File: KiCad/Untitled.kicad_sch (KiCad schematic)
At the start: 1 part

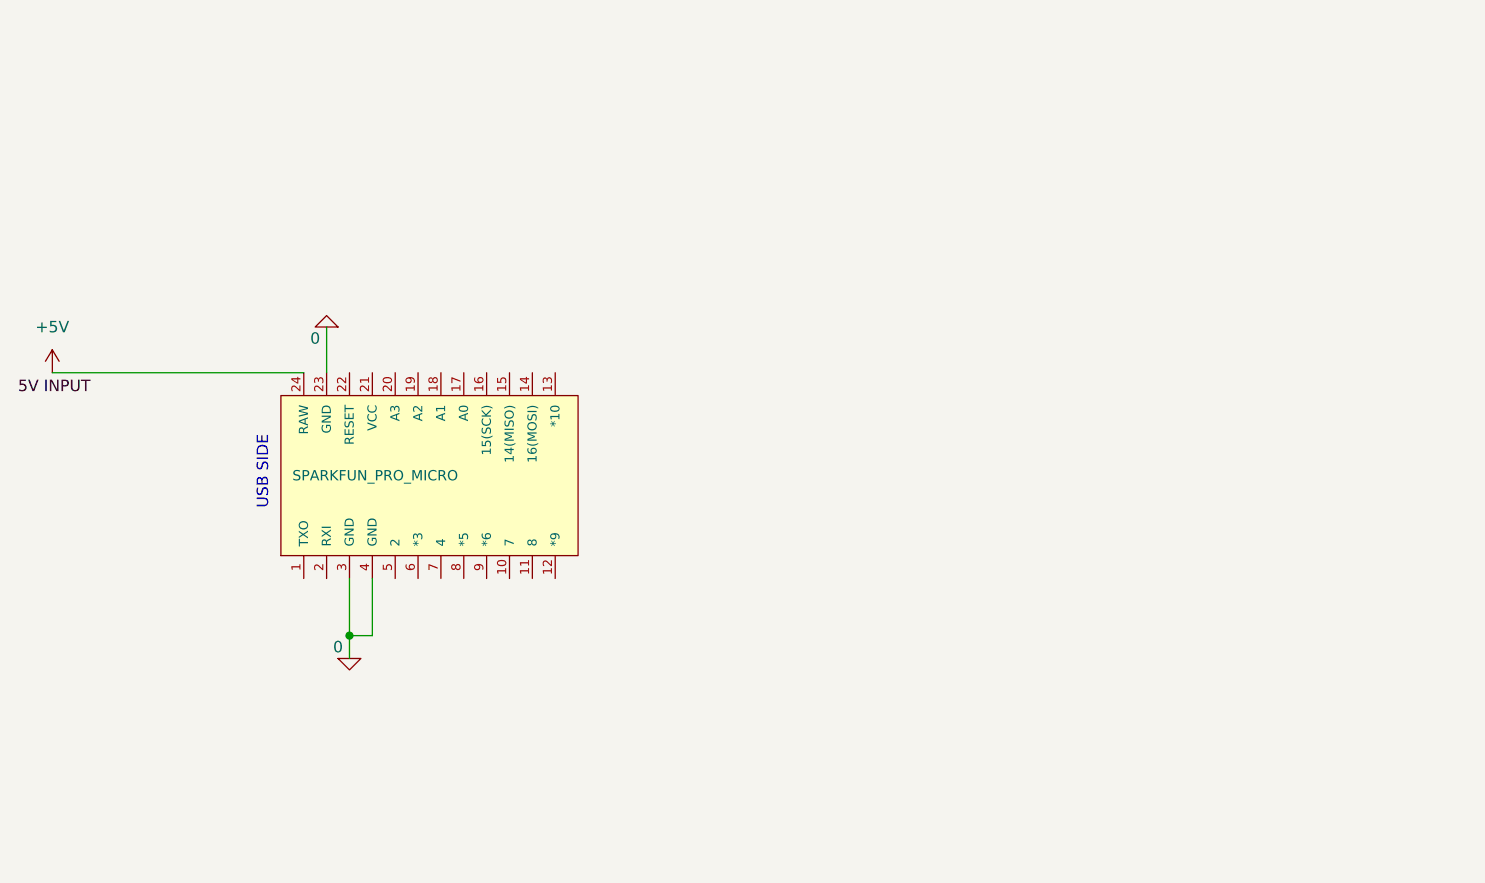
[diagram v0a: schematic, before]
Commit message: update schematics->need to add SSD1302 128x32
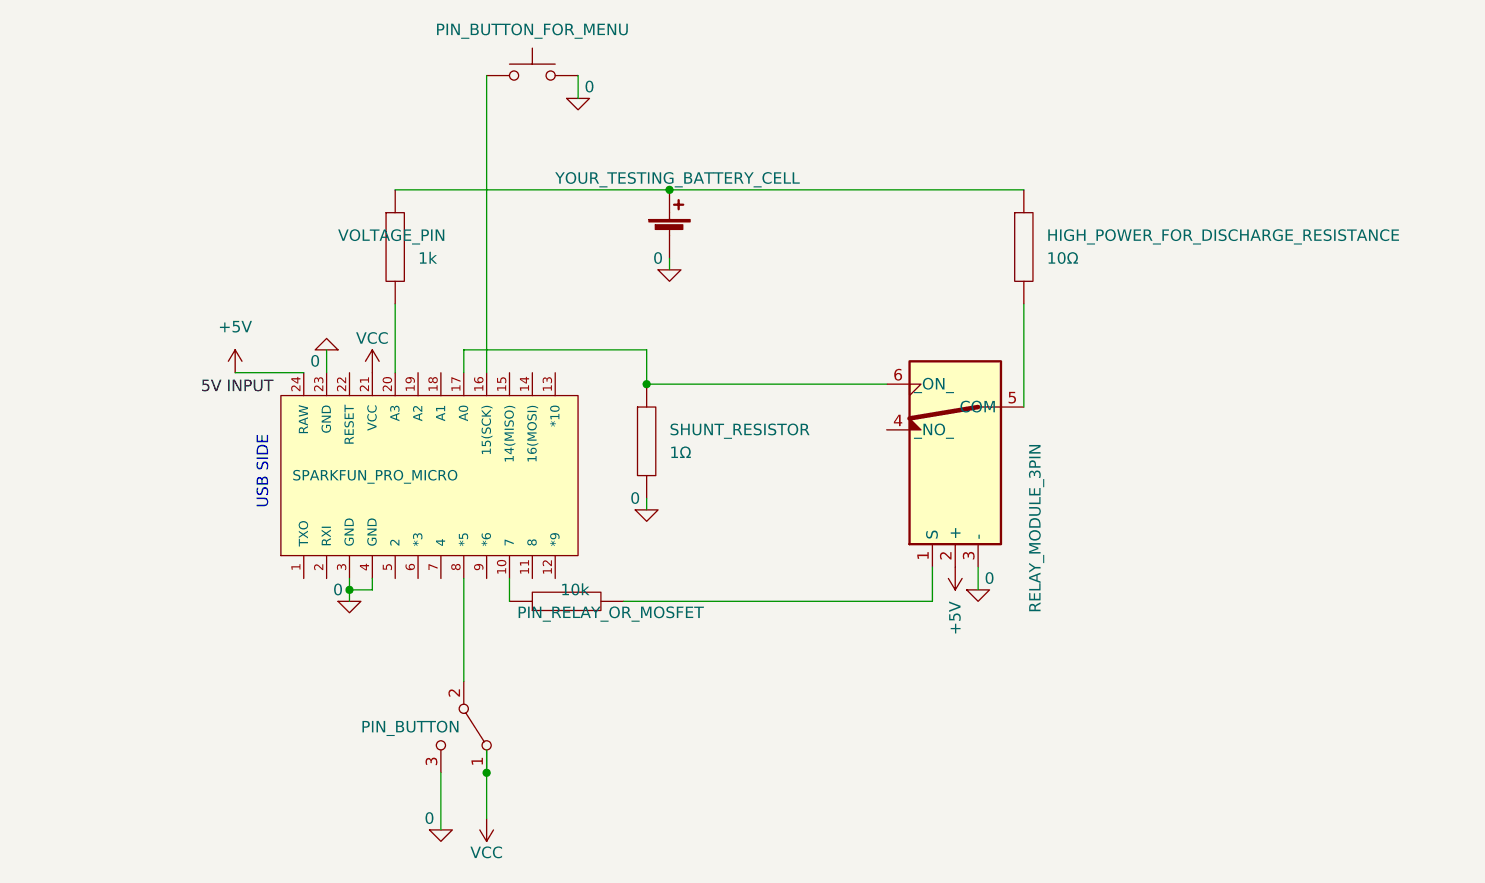
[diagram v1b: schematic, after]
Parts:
- added BT?: YOUR_TESTING_BATTERY_CELL, symbol Device:Battery_Cell
- added HIGH_POWER_FOR_DISCHARGE_RESISTANCE: 10Ω, symbol pspice:R
- added K?: RELAY_MODULE_3PIN, Relay_THT:Relay_StandexMeder_DIP_LowProfile, symbol Relay:DIPxx-1Cxx-51x
- added PIN_BUTTON_: PIN_BUTTON, symbol Switch:SW_DPDT_x2
- added PIN_RELAY_OR_MOSFET: 10k, symbol pspice:R
- added SHUNT_RESISTOR: 1Ω, symbol pspice:R
- added SW?: PIN_BUTTON_FOR_MENU, symbol Switch:SW_MEC_5G
- added VOLTAGE_PIN: 1k, symbol pspice:R
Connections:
- net +5V: now also K?.2 (+)
- net 0: now also BT?.2 (-), K?.3 (-), PIN_BUTTON_.3 (C), SHUNT_RESISTOR.2, SW?.3 (B), SW?.4 (B)
- net at B?.10 (7): now also PIN_RELAY_OR_MOSFET.1
- net at B?.16 (15(SCK)): now also SW?.1 (A), SW?.2 (A)
- net at B?.17 (A0): now also K?.6 (_ON_), SHUNT_RESISTOR.1
- net at B?.20 (A3): now also VOLTAGE_PIN.2
- net VCC: now reaches B?.21 (VCC)
- net VCC: now also PIN_BUTTON_.1 (A)
- net at B?.8 (*5): now also PIN_BUTTON_.2 (B)
- new net: BT?.1 (+), HIGH_POWER_FOR_DISCHARGE_RESISTANCE.1, VOLTAGE_PIN.1
- new net: K?.1 (S), PIN_RELAY_OR_MOSFET.2
- new net: HIGH_POWER_FOR_DISCHARGE_RESISTANCE.2, K?.5 (COM)

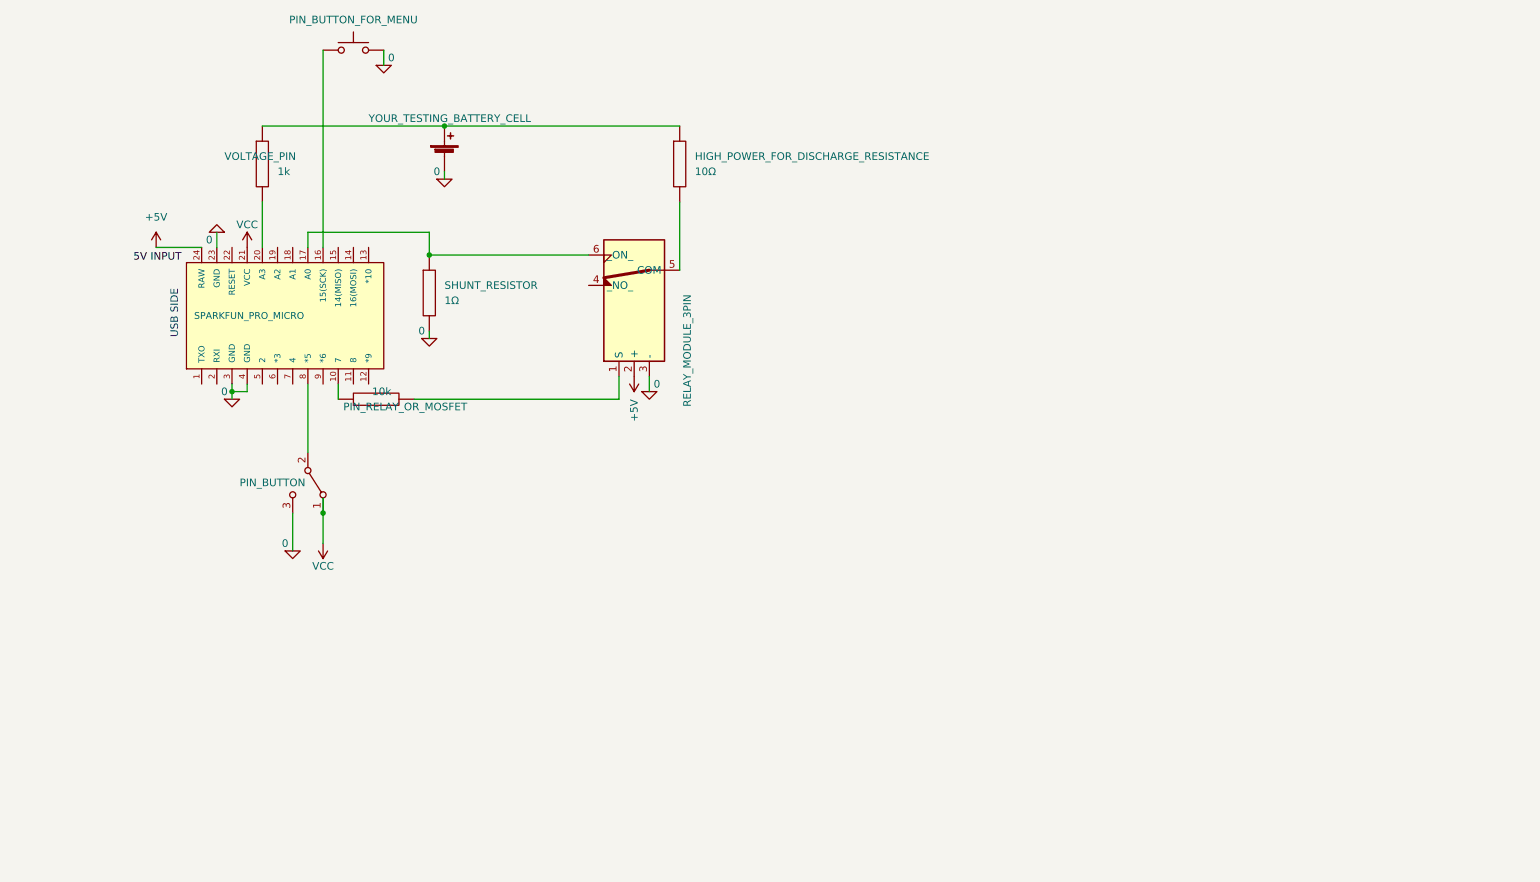
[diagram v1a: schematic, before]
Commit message: update schematics with ssd1306
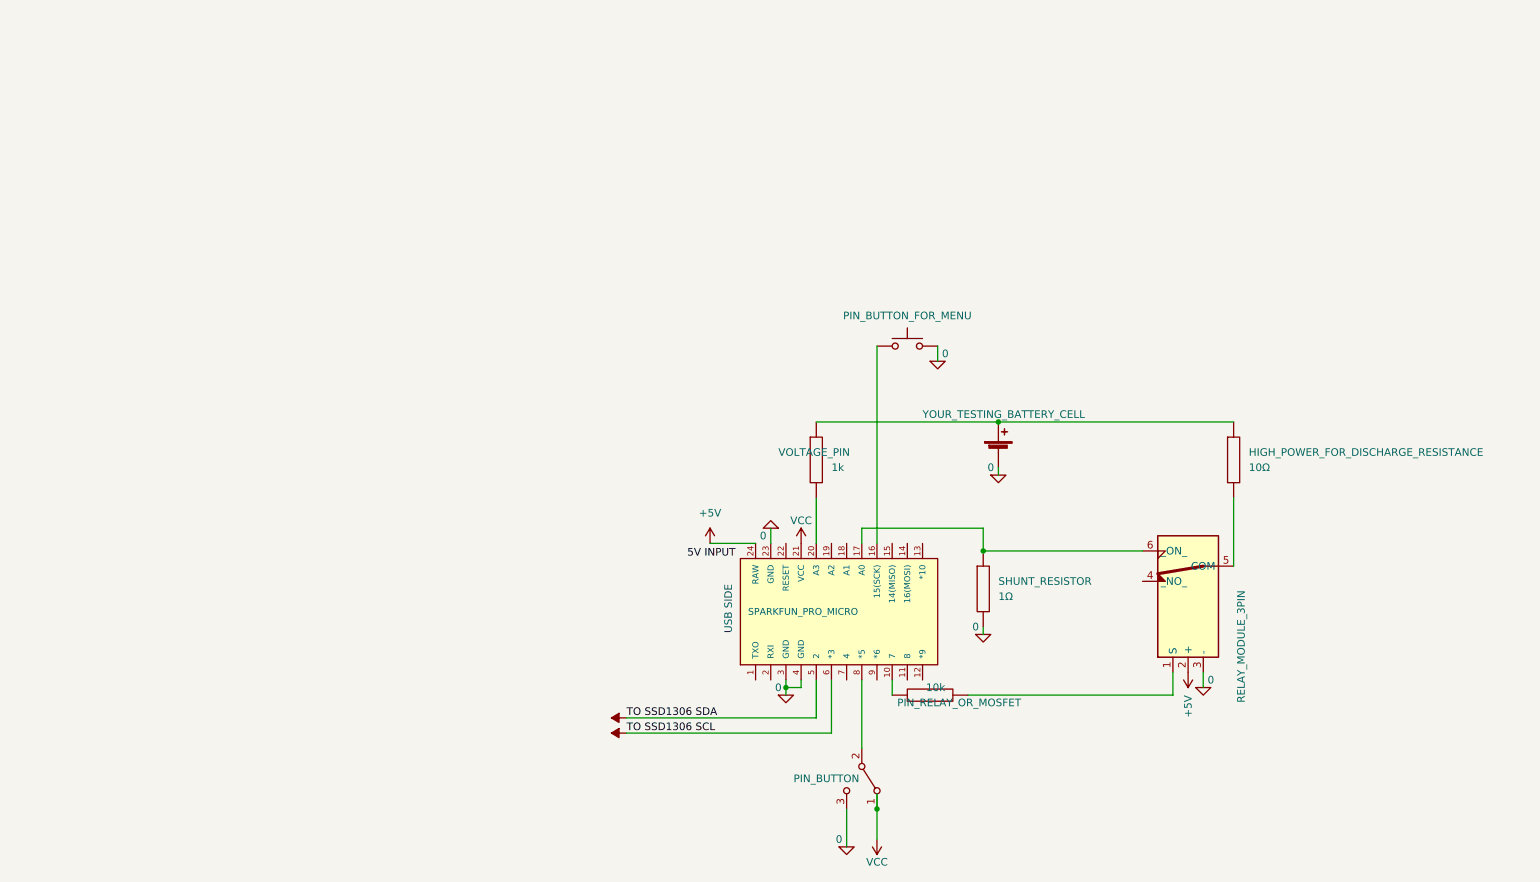
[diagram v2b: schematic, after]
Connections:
- net VSS: now reaches B?.5 (2)
- net VSS: now also B?.6 (*3)
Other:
- company: (none) -> joyel24 (JOEL M)
- title: (none) -> SimpleArduinoBatteryCapacityOLED
- moved on the sheet: HIGH_POWER_FOR_DISCHARGE_RESISTANCE, PIN_RELAY_OR_MOSFET, SHUNT_RESISTOR, VOLTAGE_PIN
